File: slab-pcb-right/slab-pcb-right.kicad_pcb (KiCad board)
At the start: 2 copper layers, 158 x 104 mm, 128 parts, among them J1 MagnetR, J2 MagnetL, J3 TRRS_R, J4 TRRS_L, J5 SSD1306, J6 Conn_01x06, SW1 RotaryEncoder, U1 Seeeduino Xiao rp2040, U2 PCA9555PW, U3 PCA9555PW, U4 ADS1110

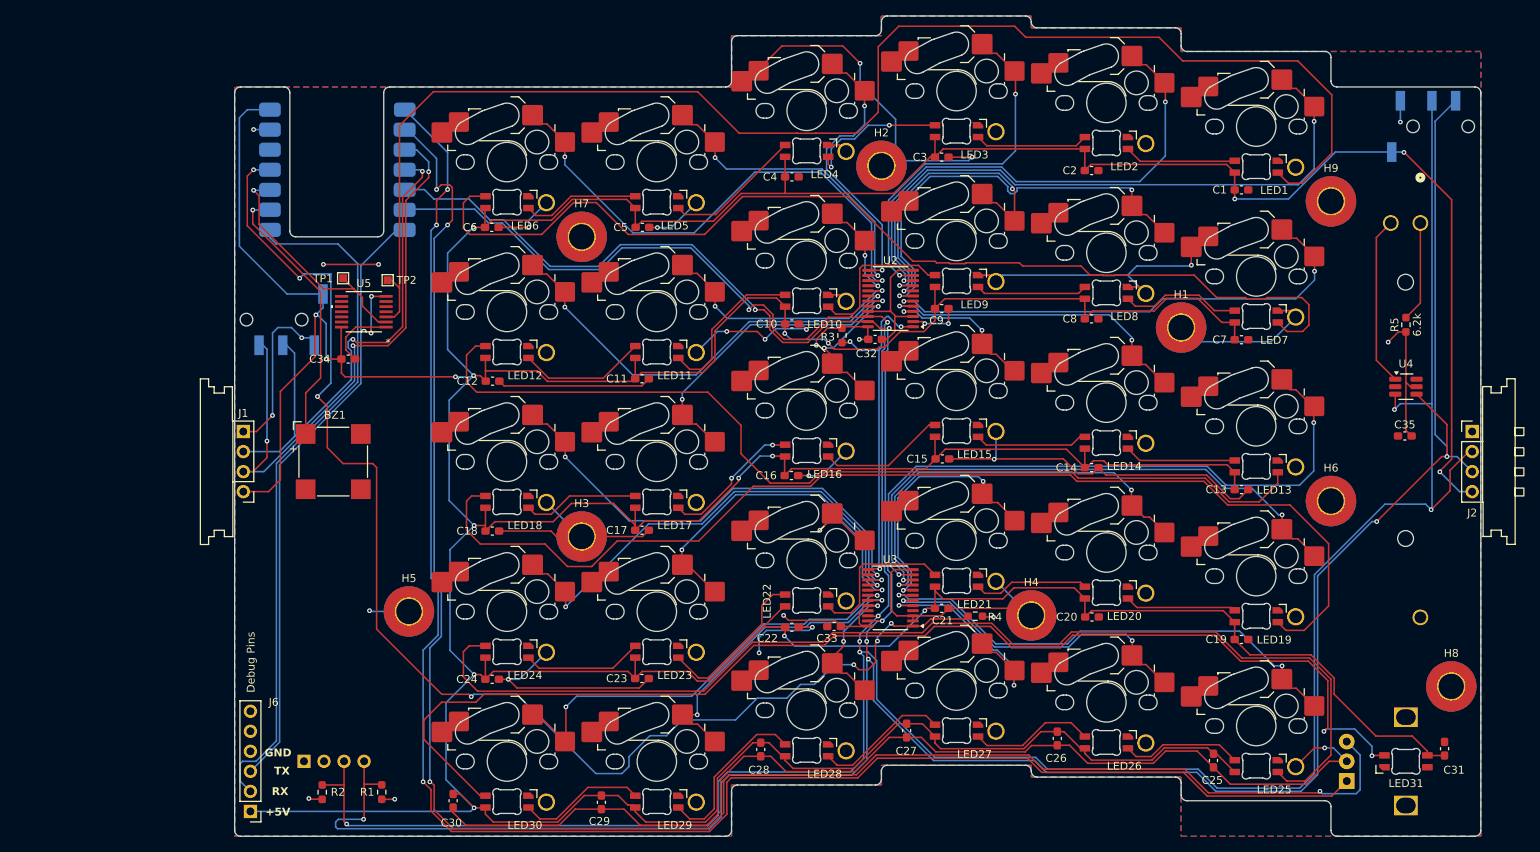
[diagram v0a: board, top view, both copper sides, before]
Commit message: feat: add User.6 as printable layout helper
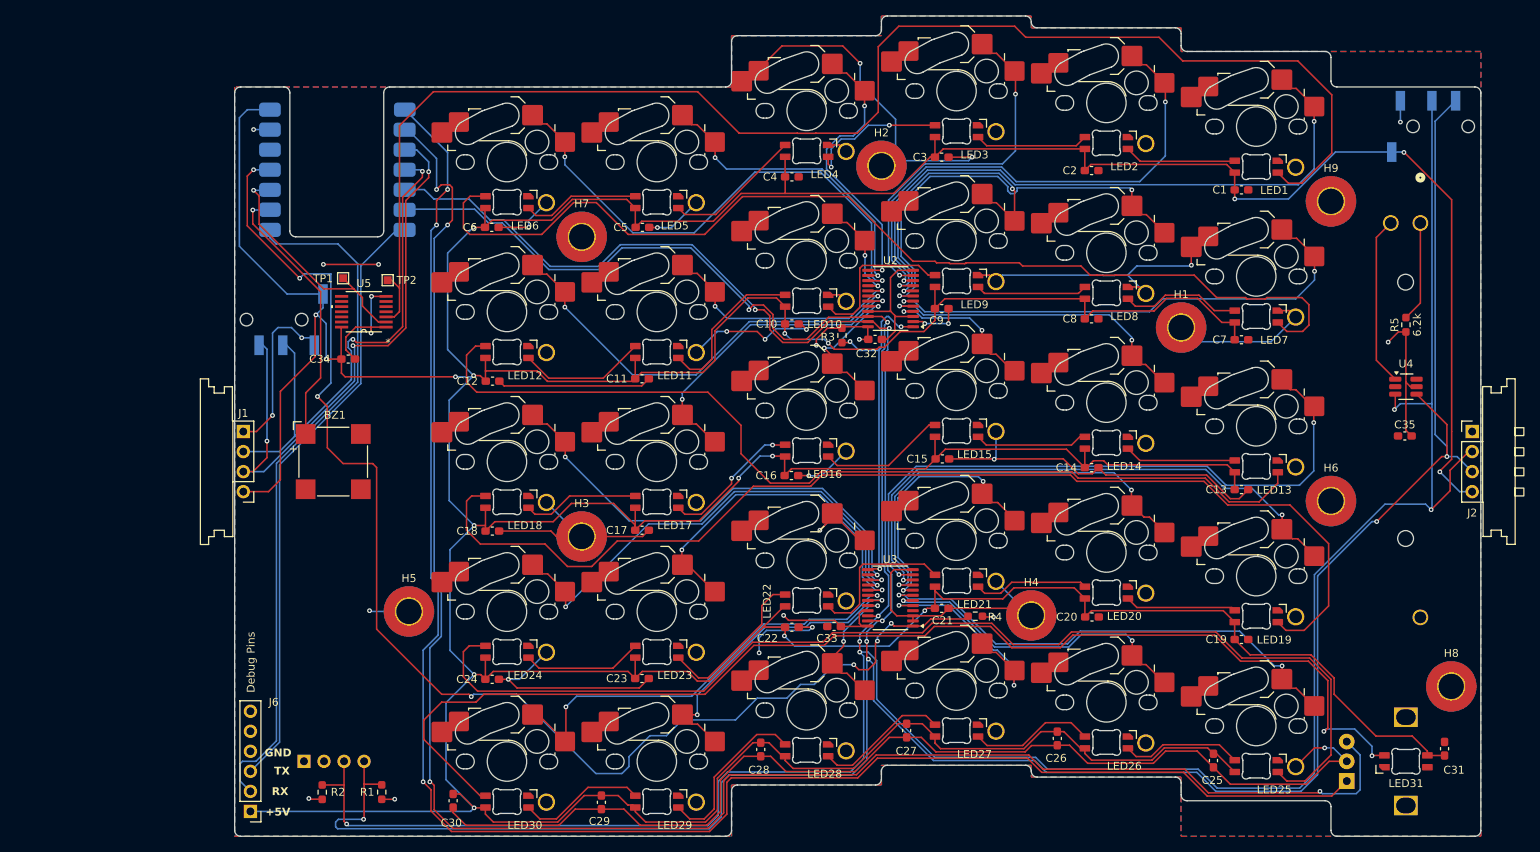
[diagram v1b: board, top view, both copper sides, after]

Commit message: feat: start on v4, updated: right-hand schematic
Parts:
- removed J6: Conn_01x06, Connector_PinHeader_2.54mm:PinHeader_1x06_P2.54mm_Vertical
- added REF**: KiCad-Logo2_8mm_SilkScreen, Symbol:KiCad-Logo2_8mm_SilkScreen, F.Cu at (81.7, 123.0)
- U5: value (none) -> SN74AHCT125PWR
- moved OSHW 12.6 mm to (91.3, 96.0)
- moved WEEE 11.0 mm to (75.0, 95.9)
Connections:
- U1 pad 14: /UART0_RX -> /EXPANDER1_INT
- U1 pad 7: /UART0_TX -> unconnected-(U1-P0-Pad7)_1
- U3 pad 13: /EXPANDER1_INT -> unconnected-(U3-IO1_0-Pad13)
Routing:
- net /UART0_RX: track 88.1 -> 0.00 mm
- net GND: track 518.7 -> 596.5 mm, vias 23 -> 27
- net /UART0_TX: track 77.3 -> 0.00 mm
- net /EXPANDER1_INT: track 43.6 -> 108.6 mm, vias 3 -> 2
- net +3V3: track 55.8 -> 83.6 mm, vias 9 -> 10
- net VBUS: track 934.4 -> 911.7 mm
- net /I2C0_SCL: track 67.2 -> 77.8 mm
- net /I2C0_SDA: track 76.9 -> 81.8 mm
- net /KEY17: track 40.0 -> 44.3 mm
- net /EXPANDER2_INT: track 167.6 -> 163.7 mm, vias 7 -> 5
- net /KEY_PIXEL_SHIFT_INPUT: track 29.4 -> 27.5 mm, vias 1 -> 0
- net Net-(LED6-DOUT): track 132.5 -> 134.1 mm
- net (no net): track 0.00 -> 1.00 mm
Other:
- board text added: "3.3"
- board text added: "Female Connector"
- board text added: "Male Connector"
- board text added: "by edwardh.dev"
- board text added: "designed by Edward Hesketh github/headblockhead"
- board text added: "interchange"
- board text added: "version"
- board text removed: "+5V"
- board text removed: "Debug Pins"
- board text removed: "RX"
- board text removed: "TX"
- board text removed: "designed by edward h"
- board text removed: "the slab keyboard"
- board text removed: "version 3.2 'nowhere'"

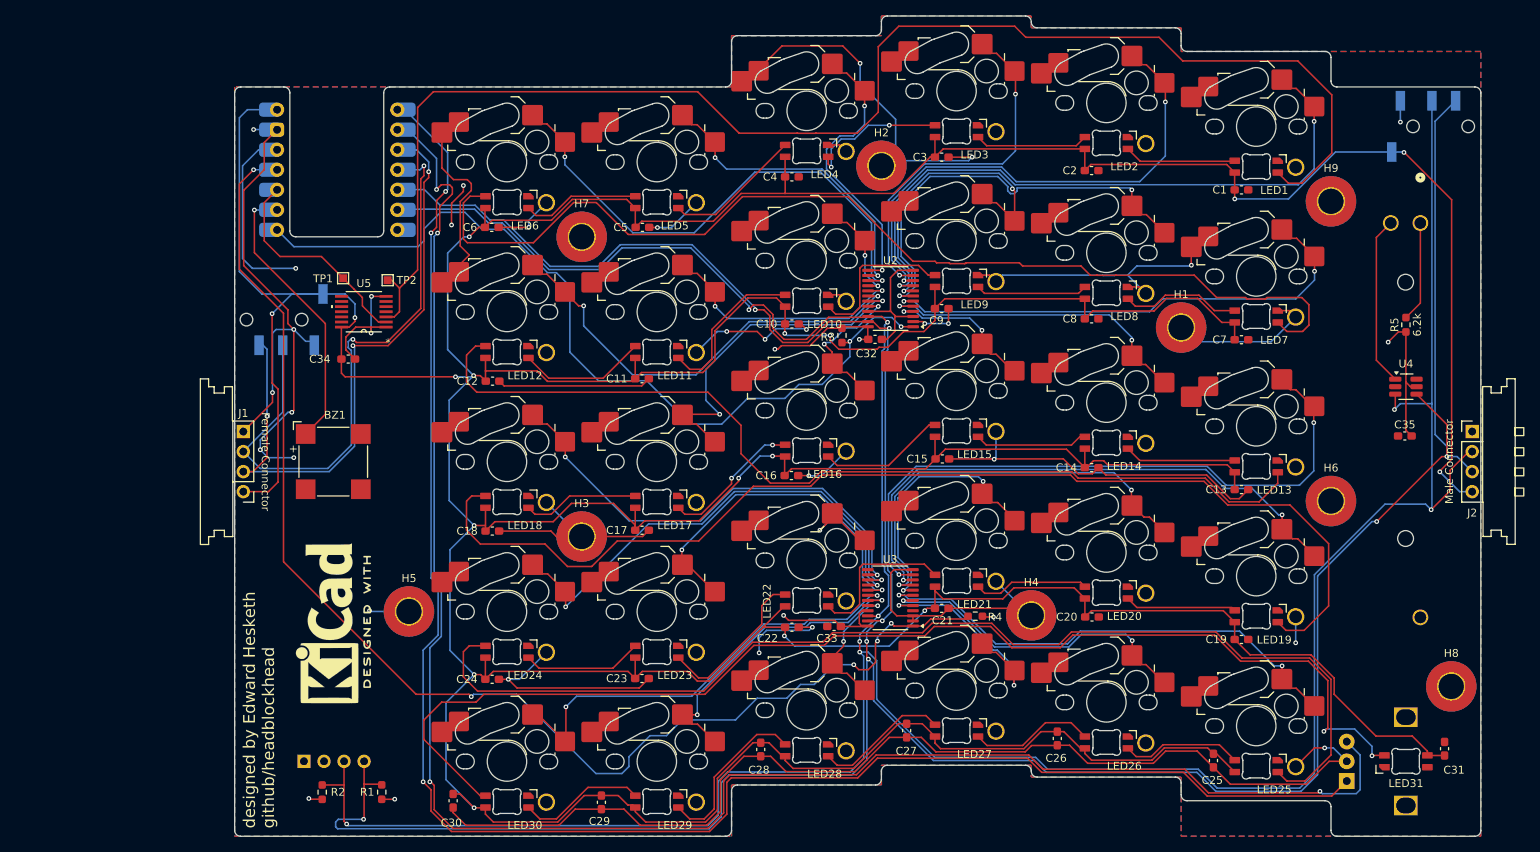
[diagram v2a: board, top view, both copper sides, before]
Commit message: feat: route most of slab-pcb-right
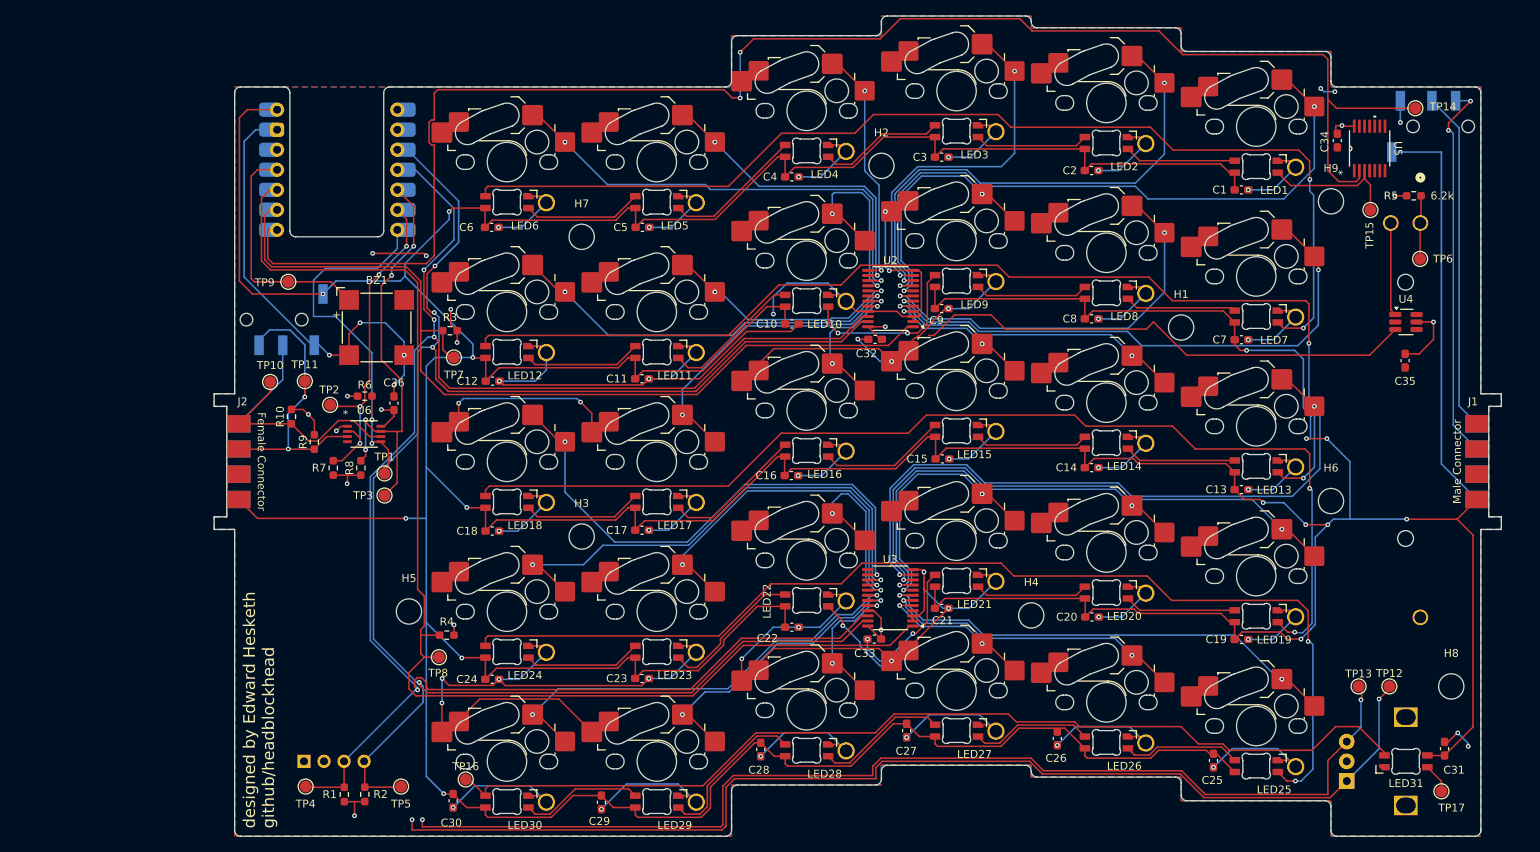
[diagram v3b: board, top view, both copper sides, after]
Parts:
- removed OSHW: OSHW-Logo2_7.3x6mm_SilkScreen, Symbol:OSHW-Logo2_7.3x6mm_SilkScreen
- removed REF**: KiCad-Logo2_8mm_SilkScreen, Symbol:KiCad-Logo2_8mm_SilkScreen
- removed WEEE: WEEE-Logo_4.2x6mm_SilkScreen, Symbol:WEEE-Logo_4.2x6mm_SilkScreen
- added C36: 100nF, Capacitor_SMD:C_0603_1608Metric_Pad1.08x0.95mm_HandSolder, F.Cu at (90.2, 95.1)
- added R10: 2.2k, Resistor_SMD:R_0603_1608Metric_Pad0.98x0.95mm_HandSolder, F.Cu at (77.2, 96.8)
- added R6: 10k, Resistor_SMD:R_0603_1608Metric_Pad0.98x0.95mm_HandSolder, F.Cu at (86.5, 94.2)
- added R7: 2.2k, Resistor_SMD:R_0603_1608Metric_Pad0.98x0.95mm_HandSolder, F.Cu at (82.5, 103.3)
- added R8: 2.2k, Resistor_SMD:R_0603_1608Metric_Pad0.98x0.95mm_HandSolder, F.Cu at (86.0, 103.3)
- added R9: 2.2k, Resistor_SMD:R_0603_1608Metric_Pad0.98x0.95mm_HandSolder, F.Cu at (80.1, 100.0)
- added TP10: TestPoint, TestPoint:TestPoint_Pad_D1.5mm, F.Cu at (74.5, 92.4)
- added TP11: TestPoint, TestPoint:TestPoint_Pad_D1.5mm, F.Cu at (78.9, 92.3)
- added TP12: TestPoint, TestPoint:TestPoint_Pad_D1.5mm, F.Cu at (216.4, 131.0)
- added TP13: TestPoint, TestPoint:TestPoint_Pad_D1.5mm, F.Cu at (212.5, 131.0)
- added TP14: TestPoint, TestPoint:TestPoint_Pad_D1.5mm, F.Cu at (219.7, 57.7)
- added TP15: TestPoint, TestPoint:TestPoint_Pad_D1.5mm, F.Cu at (214.0, 70.6)
- added TP16: TestPoint, TestPoint:TestPoint_Pad_D1.5mm, F.Cu at (99.3, 142.8)
- added TP17: TestPoint, TestPoint:TestPoint_Pad_D1.5mm, F.Cu at (223.0, 144.3)
- added TP3: TestPoint, TestPoint:TestPoint_Pad_D1.5mm, F.Cu at (89.0, 106.8)
- added TP4: TestPoint, TestPoint:TestPoint_Pad_D1.5mm, F.Cu at (79.0, 143.7)
- added TP5: TestPoint, TestPoint:TestPoint_Pad_D1.5mm, F.Cu at (91.1, 143.7)
- added TP6: TestPoint, TestPoint:TestPoint_Pad_D1.5mm, F.Cu at (220.3, 76.8)
- added TP7: TestPoint, TestPoint:TestPoint_Pad_D1.5mm, F.Cu at (97.8, 89.3)
- added TP8: TestPoint, TestPoint:TestPoint_Pad_D1.5mm, F.Cu at (95.9, 127.3)
- added TP9: TestPoint, TestPoint:TestPoint_Pad_D1.5mm, F.Cu at (76.8, 79.7)
- added U6: TCA4307DGKR, CustomFootprints:SOIC8_DGK_TEX, F.Cu at (86.4, 99.0)
- H1, H2, H3, H4, H5, H6, H7, H8, H9: footprint MountingHole:MountingHole_3.2mm_M3_Pad_TopBottom -> MountingHole:MountingHole_3.2mm_M3
- J1: value MagnetR -> Conn_01x04; footprint CustomFootprints:5358_mag_connector_1x4_pads -> CustomFootprints:MagneticSlot_Right
- J2: value MagnetL -> Conn_01x04; footprint CustomFootprints:5358_mag_connector_1x4_pins -> CustomFootprints:MagneticSlot_Left
- J3: value TRRS_R -> TRRS_L
- J4: value TRRS_L -> TRRS_R
- RV1: value R_Potentiometer -> Slider
- SW1: footprint Rotary_Encoder:RotaryEncoder_Alps_EC12E_Vertical_H20mm -> CustomFootprints:RotaryEncoder_Alps_EC12E_Vertical_H20mm_Custom
- TP1: value NPIXEL_SHIFT -> TestPoint; footprint TestPoint:TestPoint_Pad_1.0x1.0mm -> TestPoint:TestPoint_Pad_D1.5mm
- TP2: value NPIXEL_IN -> TestPoint; footprint TestPoint:TestPoint_Pad_1.0x1.0mm -> TestPoint:TestPoint_Pad_D1.5mm
- moved J1 156.9 mm to (228.0, 102.5)
- moved J2 156.9 mm to (70.0, 102.5)
- moved U5 129.2 mm to (213.9, 62.8), turned to 90 degrees
- moved C34 128.4 mm to (209.8, 61.8), turned to 90 degrees
- moved R4 67.0 mm to (96.9, 124.5)
- moved R3 49.7 mm to (97.3, 85.9), turned to 180 degrees
- moved TP1 25.3 mm to (89.0, 104.0), turned to 0 degrees
- moved BZ1 17.9 mm to (88.0, 85.5)
- moved TP2 17.4 mm to (82.1, 95.3), turned to 0 degrees
- moved R5 16.4 mm to (219.5, 68.8), turned to 0 degrees
- moved C35 9.55 mm to (218.4, 89.7), turned to 90 degrees
- moved U4 8.20 mm to (218.5, 84.8)
- moved R2 5.41 mm to (86.5, 144.7)
- moved C33 5.35 mm to (151.1, 125.0), turned to 0 degrees
- moved R1 4.76 mm to (83.9, 144.7)
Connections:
- net /ENCODER_A renamed /ROT_A
- net /ENCODER_B renamed /ROT_B
- net Net-(LED30-DOUT) renamed /RGBLEDARRAY_OUTPUT
- C32 pad 1: +3V3 -> GND
- C32 pad 2: GND -> +3V3
- C33 pad 1: +3V3 -> GND
- C33 pad 2: GND -> +3V3
- C34 pad 2: VBUS -> +3V3
- J1 pad 1: GND -> /I2C_BUS_SDA
- J1 pad 2: /I2C0_SCL -> /I2C_BUS_SCL
- J1 pad 3: /I2C0_SDA -> GND
- J2 pad 1: GND -> /I2C_BUS_SDA
- J2 pad 2: /I2C1_SCL -> /I2C_BUS_SCL
- J2 pad 3: /I2C1_SDA -> GND
- J3 pad R1: /I2C0_SCL -> /I2C_BUS_SDA
- J3 pad R2: /I2C0_SDA -> /I2C_BUS_SCL
- J4 pad R1: /I2C1_SCL -> /I2C_BUS_SDA
- J4 pad R2: /I2C1_SDA -> /I2C_BUS_SCL
- J5 pad 3: /I2C1_SCL -> /I2C0_SCL
- J5 pad 4: /I2C1_SDA -> /I2C0_SDA
- LED1 pad 3: /KEY_PIXEL_INPUT -> /SHIFTER_OUTPUT
- LED31 pad 2: unconnected-(LED31-DOUT-Pad2) -> Net-(LED31-DOUT)
- R1 pad 2: /I2C1_SDA -> /I2C0_SCL
- R2 pad 2: /I2C1_SCL -> /I2C0_SDA
- TP1 pad 1: /KEY_PIXEL_SHIFT_INPUT -> /I2C1_RDY
- TP2 pad 1: /KEY_PIXEL_INPUT -> /I2C1_SCL
- U1 pad 11: /EXPANDER2_INT -> /BUZZER
- U1 pad 12: /KEY_PIXEL_SHIFT_INPUT -> /EXPANDER2_INT
- U1 pad 13: /BUZZER -> /EXPANDER1_INT
- U1 pad 14: /EXPANDER1_INT -> /SHIFTER_INPUT
- U1 pad 7: unconnected-(U1-P0-Pad7)_1 -> /I2C1_RDY
- U2 pad 22: /I2C1_SCL -> /I2C0_SCL
- U2 pad 23: /I2C1_SDA -> /I2C0_SDA
- U3 pad 22: /I2C1_SCL -> /I2C0_SCL
- U3 pad 23: /I2C1_SDA -> /I2C0_SDA
- U4 pad 3: /I2C1_SCL -> /I2C0_SCL
- U4 pad 4: /I2C1_SDA -> /I2C0_SDA
- U5 pad 14: VBUS -> +3V3
- U5 pad 2: /KEY_PIXEL_SHIFT_INPUT -> /SHIFTER_INPUT
- U5 pad 3: /KEY_PIXEL_INPUT -> /SHIFTER_OUTPUT
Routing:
- net /I2C1_SCL: track 397.6 -> 43.4 mm, vias 8 -> 4
- net /I2C1_SDA: track 397.6 -> 53.9 mm, vias 8 -> 4
- net /I2C0_SCL: track 77.8 -> 292.4 mm, vias 2 -> 4
- net /SHIFTER_INPUT: track 0.00 -> 203.3 mm, vias 0 -> 2
- net /KEY_PIXEL_INPUT: track 180.1 -> 0.00 mm
- net /I2C0_SDA: track 81.8 -> 226.7 mm, vias 3 -> 4
- net /I2C_BUS_SCL: track 0.00 -> 87.1 mm, vias 0 -> 4
- net /ROT_B: track 226.9 -> 140.4 mm, vias 4 -> 2
- net /I2C_BUS_SDA: track 0.00 -> 83.4 mm
- net /ROT_A: track 219.8 -> 144.1 mm, vias 3 -> 2
- net GND: track 596.5 -> 659.3 mm, vias 27 -> 51
- net /I2C1_RDY: track 0.00 -> 48.9 mm, vias 0 -> 2
- net /KEY_PIXEL_SHIFT_INPUT: track 27.5 -> 0.00 mm
- net /RGBLEDARRAY_OUTPUT: track 153.5 -> 127.0 mm, vias 2 -> 0
- net +3V3: track 83.6 -> 60.0 mm, vias 10 -> 16
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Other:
- outline, holes or cut-outs redrawn
- board text added: "4.0"
- board text removed: "3.3"
